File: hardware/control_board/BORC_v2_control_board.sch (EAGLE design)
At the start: 170 parts, among them J1 USB Female Type C Connector, J2 QWIIC_RIGHT_ANGLE, J3 M20-8900405, J5 S2B-XH-A(LF)(SN), Q1 SSM3J374R,LF, Q10 BSS138PW,115, Q11 SSM3J374R,LF, Q16 UMT3904T106, Q2 SSM3J374R,LF, Q3 BSS138PW,115, Q4 UMT3904T106, Q5 SSM3J374R,LF, Q6 UMT3904T106, Q7 SSM3J374R,LF, Q9 BSS138PW,115, SW1 SPST_TACT-KMR2, U1 ATMEGA1284P-MU, U11 INA219AIDCNR, U2 SHT40-BD1B, U3 PCA9685, U4 MCP1703CB, U5 POLOLU_STEPUP_U3V40F5, U6 915MHz, U7 AT25F512BJEDEC_3.9MM, U8 FT231XQ-R, U9 MCP73833T-AMI/MF, Y1 16 MHz

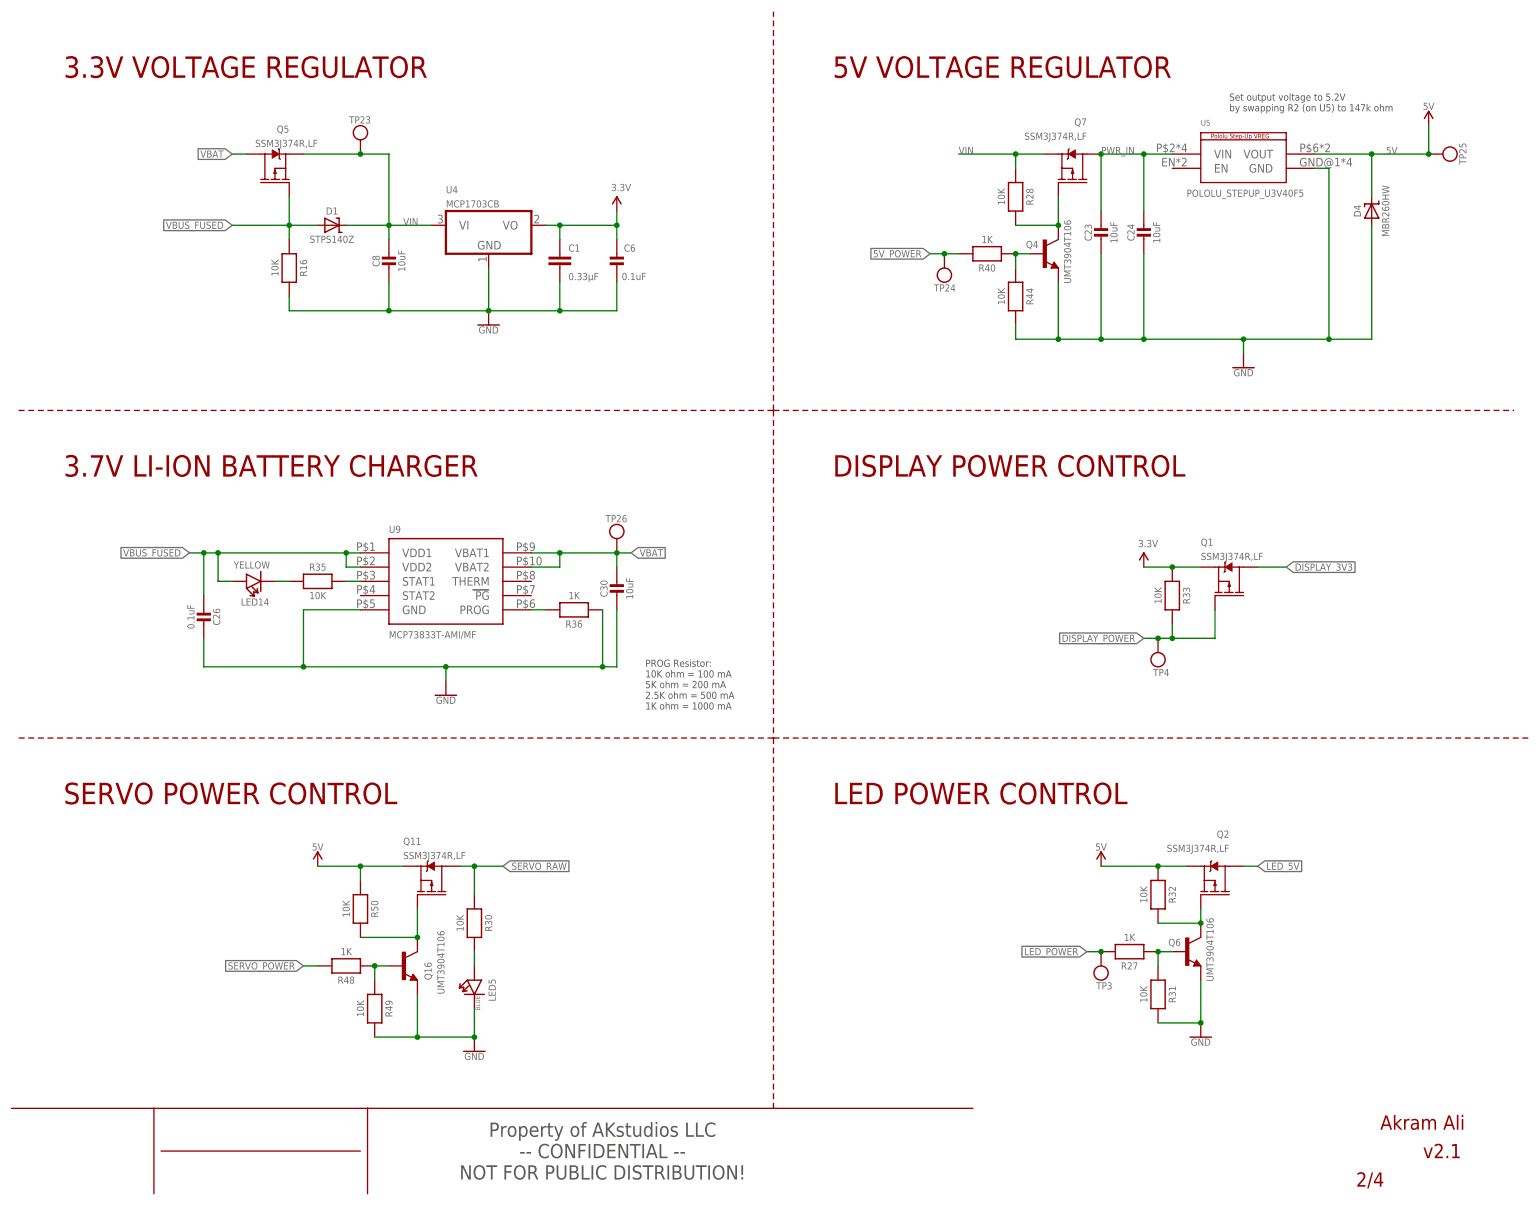
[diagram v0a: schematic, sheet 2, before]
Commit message: v2.2 - bug fixes
- Fixed display power circuit with PNP (active low)
- Replace charger with MCP73781 (can toggle between 500mA and 1000mA with jumper)
- Fixed battery JST with PH connector
- Fixed 5V switch to switch before 5V boost instead of after to avoid voltage drop
- Merged 5V power with LED power
- Connected USB shield to ground
- Connected rotary encoder shield to ground
- Removed blue LED from 5V power to avoid voltage drop
- Thickened some power traces where needed
- Minor adjustments to traces, component placement and silkscreen to accommodate design changes
- Thickened mounting holes
- Added visible ground silkscreen for servo
- Renamed LEDs to match dotstar in code
- Better info in schematics where needed
- Updated dimensions, schematics, gerber, renders, BOM, 3D step files
- ERC/DRC done
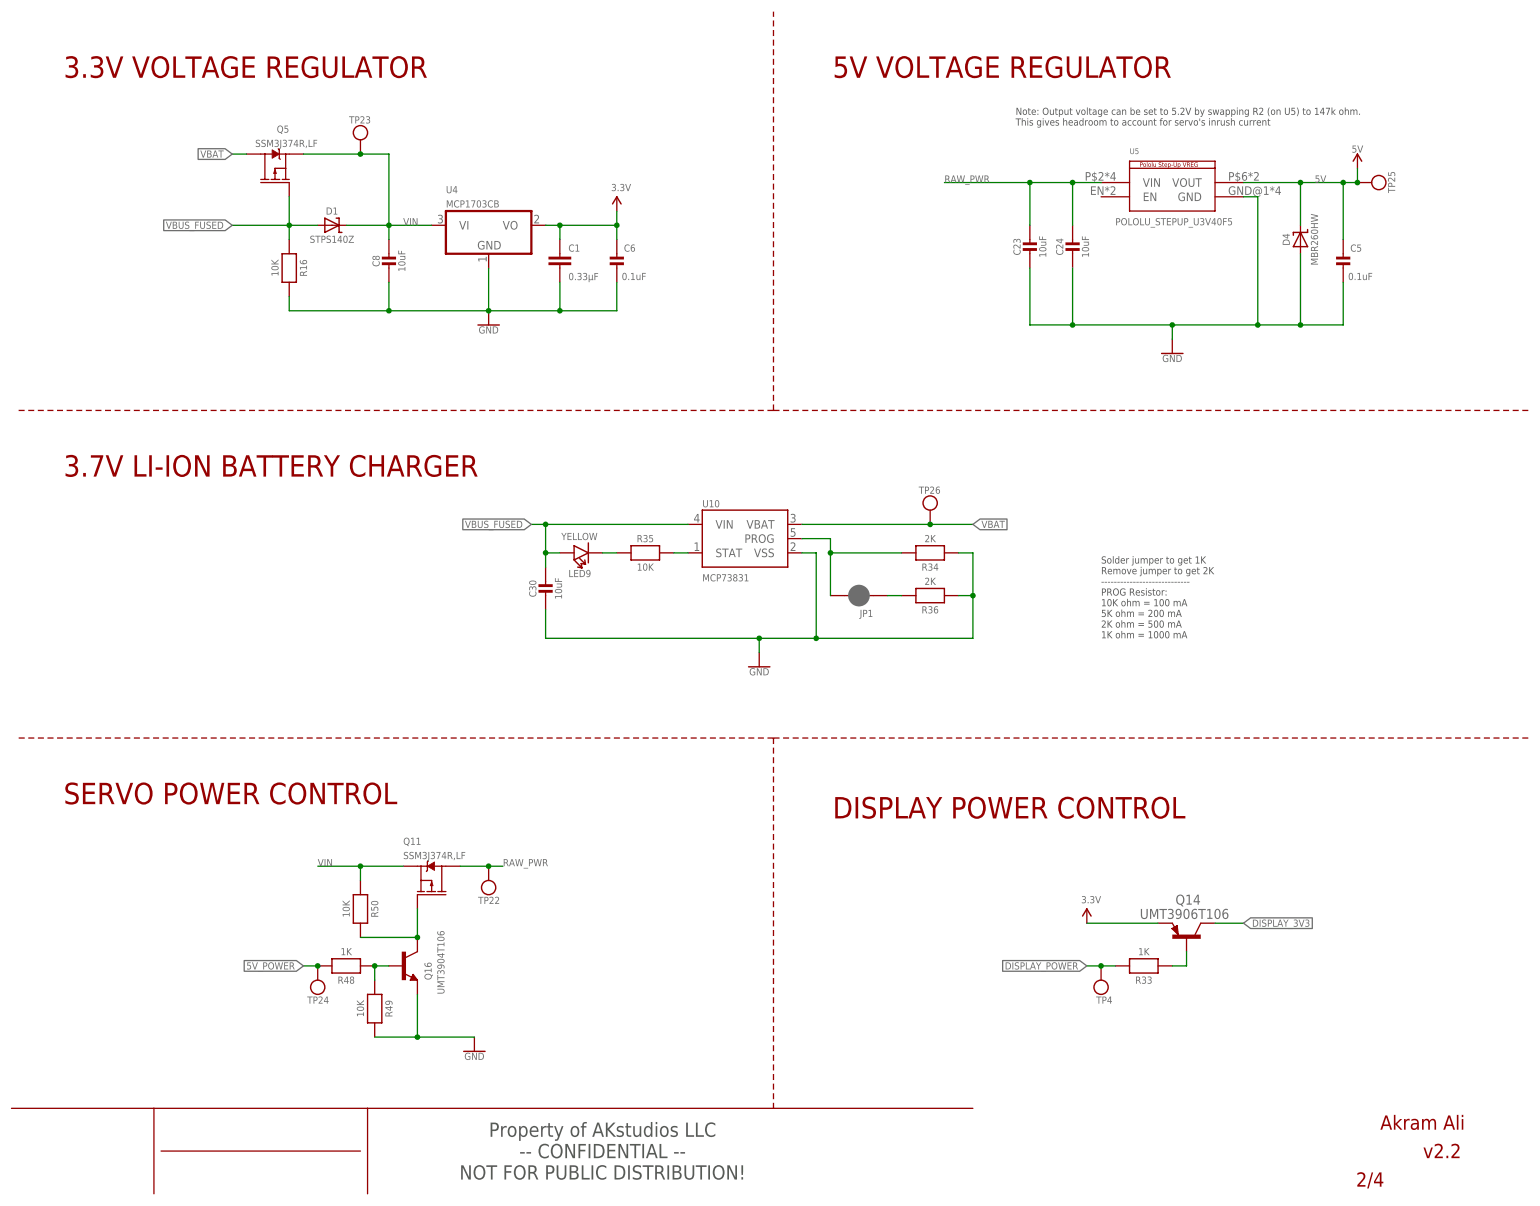
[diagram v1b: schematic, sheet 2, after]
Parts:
- removed C26: 0.1uF, Adafruit Feather 32u4 Bluefruit LE:MICROBUILDER_CAP_CERAMIC_0402MP
- removed LED10, LED11: APA102, microbuilder:APA1022020
- removed LED12: GREEN, Seeed-LED:SMD-LED-CLEAR-BLUE(0402)
- removed LED14: YELLOW, Seeed-LED:SMD-LED-CLEAR-BLUE(0402)
- removed MH1, U$3, U$4, U$7: MOUNTINGHOLE2.5, ADS1x15:MOUNTINGHOLE2.5
- removed Q1, Q2, Q7: SSM3J374R,LF, MOSFETs:MOSFET-PCH-BSS84
- removed Q4, Q6: UMT3904T106, SOT65P210X100-3N:UMT3904T106
- removed R27, R40: 1K, Adafruit Feather 32u4 Bluefruit LE:MICROBUILDER_RESISTOR_0402MP
- removed R28, R30, R31, R32, R44: 10K, Adafruit Feather 32u4 Bluefruit LE:MICROBUILDER_RESISTOR_0402MP
- removed TP3: RX, Adafruit Feather 32u4 Bluefruit LE:MICROBUILDER_TESTPOINTROUND1MM
- removed U9: MCP73833T-AMI/MF, microbuilder:MCP73833DFN
- added C5: 0.1uF, Adafruit Feather 32u4 Bluefruit LE:MICROBUILDER_CAP_CERAMIC_0402MP
- added JP1: JUMPER-SMT_2_NC_PASTE_SILK, SparkFun-Jumpers:JUMPER-SMT_2_NC_PASTE_SILK
- added LED0, LED2, LED3: APA102, microbuilder:APA1022020
- added Q14: UMT3906T106, UMT390X:UMT3906T106
- added R34: 2K, Adafruit Feather 32u4 Bluefruit LE:MICROBUILDER_RESISTOR_0402MP
- added TP22: RAW_PWR, Adafruit Feather 32u4 Bluefruit LE:MICROBUILDER_TESTPOINTROUND1MM
- added U$10, U$11, U$8, U$9: MICROBUILDER_MOUNTINGHOLE2.5_THICK, Adafruit Feather 32u4 Bluefruit LE:MICROBUILDER_MOUNTINGHOLE2.5_THICK
- added U10: MCP73831, SparkFun:MCP73831
- J5: value S2B-XH-A(LF)(SN) -> (none); device S2B-XH-A_LF__SN_:S2B-XH-A(LF)(SN) -> adafruit:JST_2PIN-THM-RA; MPN (none) -> S2B-PH-K-S
- LED1: value RED -> APA102; device Seeed-LED:SMD-LED-CLEAR-BLUE(0402) -> microbuilder:APA1022020; MPN IN-S42ATR -> APA102-2020
- LED5: value BLUE -> APA102; device Seeed-LED:SMD-LED-CLEAR-BLUE(0402) -> microbuilder:APA1022020; MPN IN-S42ATB -> APA102-2020
- LED7: value APA102 -> RED; device microbuilder:APA1022020 -> Seeed-LED:SMD-LED-CLEAR-BLUE(0402); MPN APA102-2020 -> IN-S42ATR
- LED8: value APA102 -> GREEN; device microbuilder:APA1022020 -> Seeed-LED:SMD-LED-CLEAR-BLUE(0402); MPN APA102-2020 -> IN-S42ATG
- LED9: value APA102 -> YELLOW; device microbuilder:APA1022020 -> Seeed-LED:SMD-LED-CLEAR-BLUE(0402); MPN APA102-2020 -> IN-S42ATY
- R33: value 10K -> 1K; MPN RC0402FR-7W10KL -> RC0402FR-071KL
- R36: value 1K -> 2K; MPN RC0402FR-071KL -> RC0402FR-072KL
- TP24: value RX -> 5V_POWER
- renumbered LED13 to LED6
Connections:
- removed net LED_5V: C20.1, C22.1, LED10.VDD, LED11.VDD, LED4.VDD, LED7.VDD, LED8.VDD, LED9.VDD, Q2.D1, R45.1, R47.1
- removed net LED_POWER: R27.2, TP3.P$1, U1.PC5_[TDI/PCINT21]
- removed net N$18: Q2.G1, Q6.C, R32.2
- removed net N$20: Q6.B, R27.1, R31.1
- removed net N$27: R36.2, U9.PROG
- removed net N$31: Q4.C, Q7.G1, R28.2
- removed net N$34: Q4.B, R40.1, R44.1
- removed net N$46: LED5.+, R30.2
- removed net PWR_IN: C23.1, C24.1, Q7.D1, U5.VIN
- removed net SERVO_POWER: R48.2, U1.PC3_[PCINT19/TMS]
- removed net SERVO_RAW: Q11.D1, R30.1, R39.2, R41.1, TP30.P$1
- new net N$19: Q14.B, R33.1
- new net N$21: JP1.2, R34.2, U10.PROG
- new net N$22: JP1.1, R36.2
- new net RAW_PWR: C23.1, C24.1, Q11.D1, TP22.P$1, U5.VIN
- net 5V: now also C20.1, C22.1, C5.1, LED0.VDD, LED1.VDD, LED2.VDD, LED3.VDD, LED4.VDD, LED5.VDD, R39.2, R41.1, R45.1, R47.1, TP30.P$1; no longer Q11.S1, Q2.S1, R32.1, R50.1
- net 5V_POWER: now also R48.2; no longer R40.2
- net C2: now also LED0.CKO, LED1.CKI; no longer LED4.CKO, LED7.CKI
- net C3: now also LED1.CKO, LED2.CKI; no longer LED7.CKO, LED8.CKI
- net C4: now also LED2.CKO, LED3.CKI; no longer LED8.CKO, LED9.CKI
- net C5: now also LED3.CKO, LED4.CKI; no longer LED10.CKI, LED9.CKO
- net C6: now also LED4.CKO, LED5.CKI; no longer LED10.CKO, LED11.CKI
- net D2: now also LED0.DO, LED1.DI; no longer LED4.DO, LED7.DI
- net D3: now also LED1.DO, LED2.DI; no longer LED7.DO, LED8.DI
- net D4: now also LED2.DO, LED3.DI; no longer LED8.DO, LED9.DI
- net D5: now also LED3.DO, LED4.DI; no longer LED10.DI, LED9.DO
- net D6: now also LED4.DO, LED5.DI; no longer LED10.DO, LED11.DI
- net DISPLAY_3V3: now also Q14.C; no longer Q1.D1
- net DISPLAY_POWER: no longer Q1.G1
- net GND: now also C5.2, J1.SHLD, LED0.GND, LED1.GND, LED2.GND, LED3.GND, LED5.GND, LED7.-, MT1.SHIELD, R34.1, U10.VSS; no longer C26.1, LED1.-, LED10.GND, LED11.GND, LED5.-, LED7.GND, LED8.GND, LED9.GND, Q4.E, Q6.E, R31.2, R44.2, U9.GND
- net LED_CLK_5V: now also LED0.CKI; no longer LED4.CKI
- net LED_DATA_5V: now also LED0.DI; no longer LED4.DI
- net N$10: now also LED8.-; no longer LED12.-
- net N$16: now also LED9.-; no longer LED14.-
- net N$2: now also LED7.+; no longer LED1.+
- net N$6: now also LED8.+; no longer LED12.+
- net N$9: now also U10.STAT; no longer U9.STAT1
- net VBAT: now also U10.VBAT; no longer C30.1, U9.VBAT1, U9.VBAT2
- net VBUS_FUSED: now also C30.1, LED9.+, U10.VIN; no longer C26.2, LED14.+, U9.VDD1, U9.VDD2
- net VCC: now also Q14.E; no longer Q1.S1, R33.1
- net VIN: now also Q11.S1, R50.1; no longer Q7.S1, R28.1
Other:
- note added: "Note: Output voltage can be set to 5.2V by swapping R2 (on U5) to 147k ohm. This gives headroom to account for servo's inrush current"
- note added: "Solder jumper to get 1K Remove jumper to get 2K ---------------------------- PROG Resistor: 10K ohm = 100 mA 5K ohm = 200 mA 2K ohm = 500 mA 1K ohm = 1000 mA"
- note added: "v2.2"
- note removed: "LED POWER CONTROL"
- note removed: "PROG Resistor: 10K ohm = 100 mA 5K ohm = 200 mA 2.5K ohm = 500 mA 1K ohm = 1000 mA"
- note removed: "Set output voltage to 5.2V by swapping R2 (on U5) to 147k ohm"
- note removed: "v2.1"
- moved on the sheet: C23, C24, C30, C7, D4, J2, J4, LED4, R15, R33, R35, R36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
